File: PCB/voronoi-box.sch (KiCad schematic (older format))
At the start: 31 parts, among them J1 Conn_01x02_Male, J2 Conn_01x02_Male, J3 Conn_01x03_Female, SW1 SW_Push, SW2 SW_Push, SW3 SW_DIP_x01, U1 ATtiny85-20PU

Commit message: remove old stuff from schematic, add battery protection, add a lot of components to Readme
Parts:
- removed C?: 10uF, Capacitor_SMD:C_0603_1608Metric, symbol Device:C
- removed C? (x3): 22uF, Capacitor_SMD:C_0603_1608Metric, symbol Device:C
- removed D?: LED, symbol Device:LED
- removed L?: 1UH, symbol Device:L
- removed R?: 2R, symbol Device:R
- removed R?: 0.5R, symbol Device:R
- removed R?: 10k, symbol Device:R
- removed R?: 1k, symbol Device:R
- removed SW?: SW_Push, Button_Switch_THT:SW_PUSH_6mm_H4.3mm, symbol Switch:SW_Push
- removed U?: IP5306-I2C, lcsc:ESOP-8_L4.9-W3.9-P1.27-LS6.0-BL-EP2.0, symbol LCSC:IP5306-I2C
- added JP?: SolderJumper_2_Open, symbol Jumper:SolderJumper_2_Open
- added R?: 1k, Resistor_SMD:R_0603_1608Metric_Pad1.05x0.95mm_HandSolder, symbol Device:R
- added R?: 2k, Resistor_SMD:R_0603_1608Metric_Pad1.05x0.95mm_HandSolder, symbol Device:R
- added R?: 1M, Resistor_SMD:R_0603_1608Metric_Pad1.05x0.95mm_HandSolder, symbol Device:R
- added R?: 4k, Resistor_SMD:R_0603_1608Metric_Pad1.05x0.95mm_HandSolder, symbol Device:R
- added R?: 8k, Resistor_SMD:R_0603_1608Metric_Pad1.05x0.95mm_HandSolder, symbol Device:R
- added SW? (x3): SW_Push, Button_Switch_THT:SW_PUSH_6mm_H4.3mm, symbol Switch:SW_Push
- added U?: XB8089D0, lcsc:SOIC-8_L4.9-W3.9-P1.27-LS6.0-BL-EP3.3-1, symbol LCSC:XB8089D0
- C?: value 22uF -> 0.1uF
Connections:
- net labels added: BAT+, BAT-, BAT_-, CHRG_+, CHRG_-
- net labels removed: +BATT
- wire segments 43 -> 50
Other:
- note added: "..."
- note added: "// How can it be good to have a resistor in series??"
- note added: "<= 8 MHz with any precision, so it doesn't need external oscillator\n-> set via chip fuses\n\nVBAT can be measured from VCC, keep AREF floating\n\nPB1 can PWM, PB2 has INT0, all have internal pull-up."
- note added: "Battery Protection (Optional)\n4.25 V -> 4.10 V | 2.90 V-> 3.0 V | 10.0 A"
- note added: "TODO:\n- switch via connector?"
- note added: "bridge to bypass BMS"
- note removed: "<= 8 MHz with any precision, so it doesn't need external oscillator\n-> set via chip fuses\n\nVBAT can be measured from VCC, keep AREF floating\n\nPB2 has INT0, PB1 can PWM, all have internal pull-up."
- note removed: "TODO:\n- switch via connector?\n\nIP5306:\n- Optocoupler or direct IO? "Flashlight" mode dangerous. Might work by load alone.\n- LED indicator disable or to IO?\n- No Charge control without I2C -> connect via bus? Would open up AREF"
- moved on the sheet: C?, D1, F1, J1, SW1, SW2, SW3

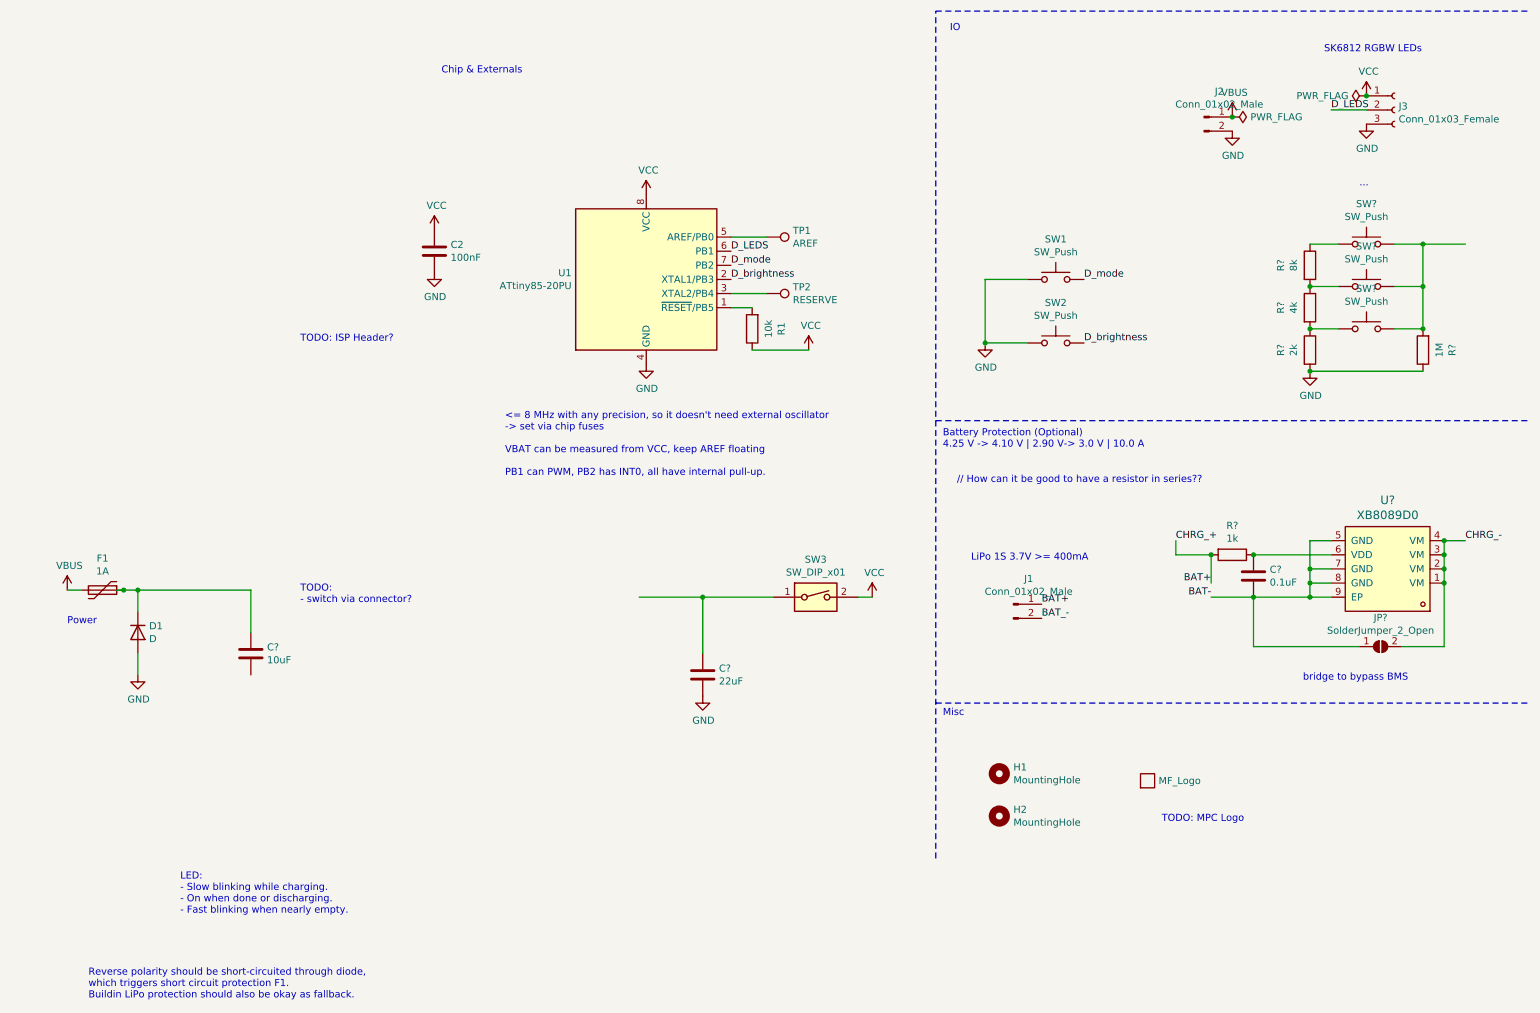
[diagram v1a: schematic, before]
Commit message: extend Readme with a huge knowledge drop, create new power path with dedicated parts, add ISP, use analog mux for buttons, try to fix CI
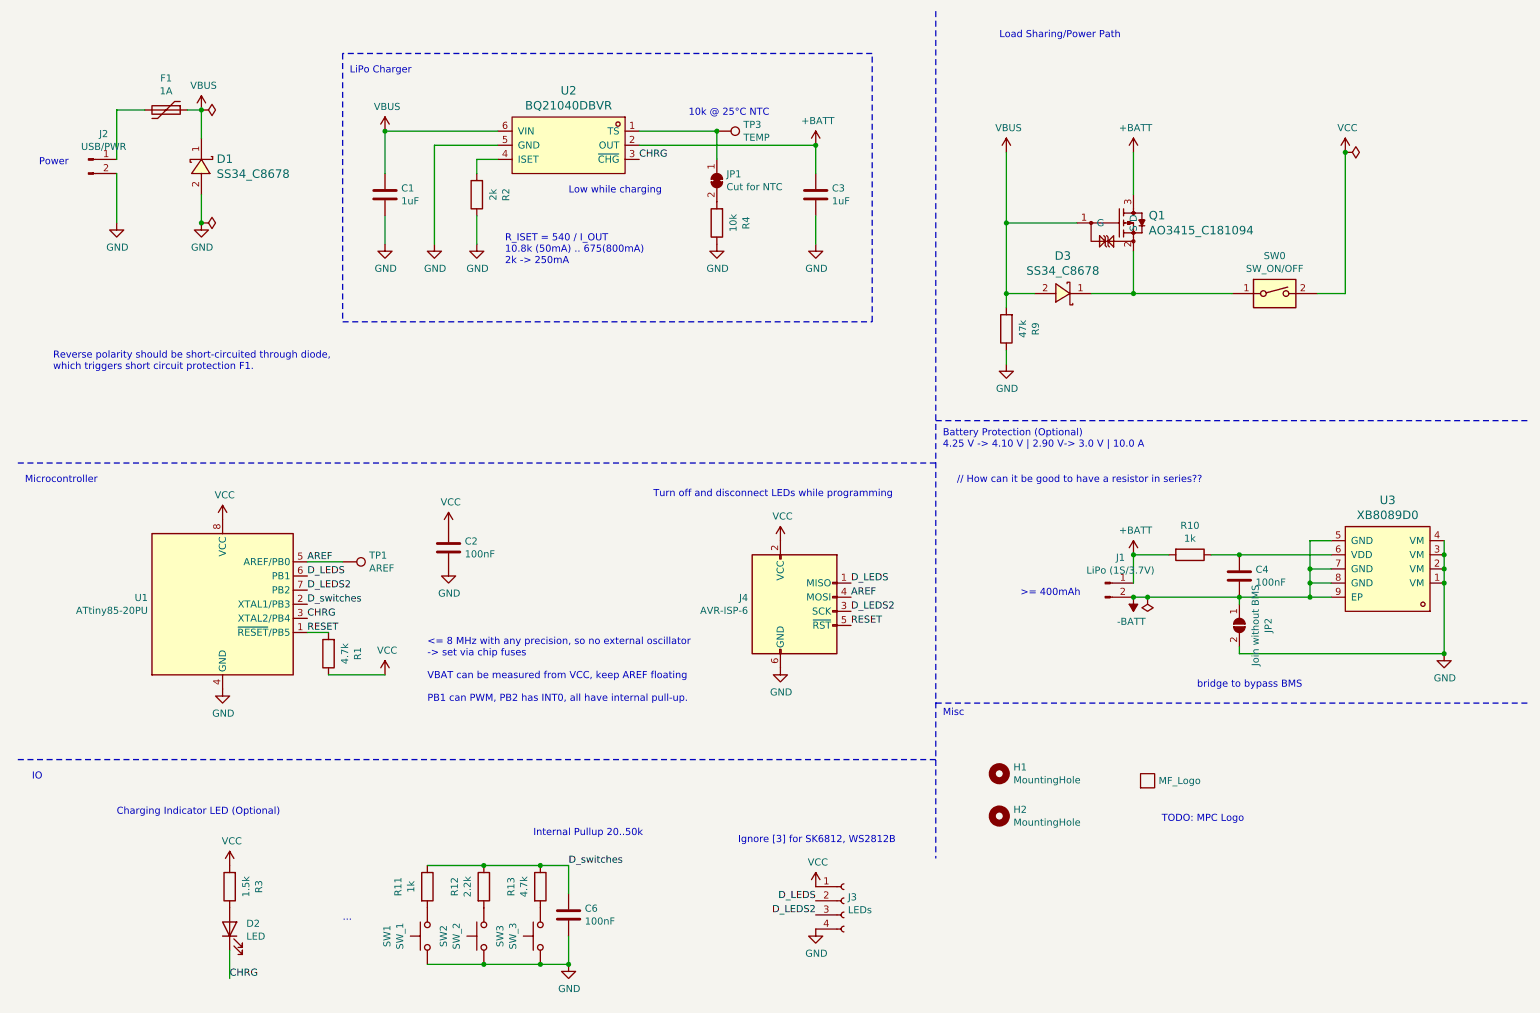
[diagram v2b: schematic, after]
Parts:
- removed C?: 22uF, Capacitor_SMD:C_0603_1608Metric, symbol Device:C
- removed D1: D, Diode_THT:D_DO-35_SOD27_P7.62mm_Horizontal, symbol Device:D
- removed J3: Conn_01x03_Female, Connector_JST:JST_XH_S3B-XH-A_1x03_P2.50mm_Horizontal, symbol Connector:Conn_01x03_Female
- removed R?: 2k, Resistor_SMD:R_0603_1608Metric_Pad1.05x0.95mm_HandSolder, symbol Device:R
- removed R?: 1M, Resistor_SMD:R_0603_1608Metric_Pad1.05x0.95mm_HandSolder, symbol Device:R
- removed R?: 4k, Resistor_SMD:R_0603_1608Metric_Pad1.05x0.95mm_HandSolder, symbol Device:R
- removed R?: 8k, Resistor_SMD:R_0603_1608Metric_Pad1.05x0.95mm_HandSolder, symbol Device:R
- removed SW? (x3): SW_Push, Button_Switch_THT:SW_PUSH_6mm_H4.3mm, symbol Switch:SW_Push
- removed TP2: RESERVE, TestPoint:TestPoint_THTPad_D2.0mm_Drill1.0mm, symbol Connector:TestPoint
- added C3: 1uF, Capacitor_SMD:C_0603_1608Metric, symbol Device:C
- added C6: 100nF, Capacitor_SMD:C_0603_1608Metric, symbol Device:C
- added D1, D3: SS34_C8678, lcsc:SMA_L4.3-W2.6-LS5.2-RD, symbol LCSC:SS34_C8678
- added D2: LED, symbol Device:LED
- added J3: LEDs, Connector_JST:JST_XH_B4B-XH-A_1x04_P2.50mm_Vertical, symbol Connector:Conn_01x04_Female
- added J4: AVR-ISP-6, Connector_PinHeader_2.54mm:PinHeader_2x03_P2.54mm_Vertical, symbol Connector:AVR-ISP-6
- added JP1: Cut for NTC, Jumper:SolderJumper-2_P1.3mm_Bridged_RoundedPad1.0x1.5mm, symbol Jumper:SolderJumper_2_Bridged
- added Q1: AO3415_C181094, lcsc:SOT-23-3_L2.9-W1.3-P1.90-LS2.4-BR, symbol LCSC:AO3415_C181094
- added R11: 1k, Resistor_SMD:R_0603_1608Metric_Pad1.05x0.95mm_HandSolder, symbol Device:R
- added R12: 2.2k, Resistor_SMD:R_0603_1608Metric_Pad1.05x0.95mm_HandSolder, symbol Device:R
- added R13: 4.7k, Resistor_SMD:R_0603_1608Metric_Pad1.05x0.95mm_HandSolder, symbol Device:R
- added R2: 2k, Resistor_SMD:R_0603_1608Metric_Pad1.05x0.95mm_HandSolder, symbol Device:R
- added R3: 1.5k, Resistor_SMD:R_0603_1608Metric_Pad1.05x0.95mm_HandSolder, symbol Device:R
- added R4: 10k, Resistor_SMD:R_0603_1608Metric_Pad1.05x0.95mm_HandSolder, symbol Device:R
- added R9: 47k, Resistor_SMD:R_0603_1608Metric_Pad1.05x0.95mm_HandSolder, symbol Device:R
- added SW3: SW_3, Button_Switch_THT:SW_PUSH_6mm_H4.3mm, symbol Switch:SW_Push
- added TP3: TEMP, TestPoint:TestPoint_THTPad_D2.0mm_Drill1.0mm, symbol Connector:TestPoint
- added U2: BQ21040DBVR, lcsc:SOT-23-6_L2.9-W1.6-P0.95-LS2.8-BR, symbol LCSC:BQ21040DBVR
- C1: renamed from C?; value 10uF -> 1uF
- C4: renamed from C?; value 0.1uF -> 100nF
- J1: value Conn_01x02_Male -> LiPo (1S/3.7V)
- J2: value Conn_01x02_Male -> USB/PWR
- JP2: renamed from JP?; value SolderJumper_2_Open -> Join without BMS; footprint (none) -> Jumper:SolderJumper-2_P1.3mm_Open_RoundedPad1.0x1.5mm
- R1: value 10k -> 4.7k
- SW0: renamed from SW3; value SW_DIP_x01 -> SW_ON/OFF
- SW1: value SW_Push -> SW_1
- SW2: value SW_Push -> SW_2
- gave numbers to parts that had none: 2
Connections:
- net labels added: +BATT, -BATT, AREF, CHRG, D_LEDS2, D_switches, RESET
- net labels removed: BAT+, BAT-, BAT_-, CHRG_+, CHRG_-, D_brightness, D_mode
- wire segments 50 -> 64
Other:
- note added: "10k @ 25°C NTC"
- note added: "<= 8 MHz with any precision, so no external oscillator\n-> set via chip fuses\n\nVBAT can be measured from VCC, keep AREF floating\n\nPB1 can PWM, PB2 has INT0, all have internal pull-up."
- note added: ">= 400mAh"
- note added: "Charging Indicator LED (Optional)"
- note added: "Ignore [3] for SK6812, WS2812B"
- note added: "Internal Pullup 20..50k"
- note added: "LiPo Charger"
- note added: "Load Sharing/Power Path"
- note added: "Low while charging"
- note added: "Microcontroller"
- note added: "R_ISET = 540 / I_OUT\n10.8k (50mA) .. 675(800mA)\n2k -> 250mA"
- note added: "Reverse polarity should be short-circuited through diode, \nwhich triggers short circuit protection F1."
- note added: "Turn off and disconnect LEDs while programming"
- note removed: "<= 8 MHz with any precision, so it doesn't need external oscillator\n-> set via chip fuses\n\nVBAT can be measured from VCC, keep AREF floating\n\nPB1 can PWM, PB2 has INT0, all have internal pull-up."
- note removed: "Chip & Externals"
- note removed: "LED: \n- Slow blinking while charging. \n- On when done or discharging. \n- Fast blinking when nearly empty."
- note removed: "LiPo 1S 3.7V >= 400mA"
- note removed: "Reverse polarity should be short-circuited through diode, \nwhich triggers short circuit protection F1. \nBuildin LiPo protection should also be okay as fallback."
- note removed: "SK6812 RGBW LEDs"
- note removed: "TODO: ISP Header?"
- note removed: "TODO:\n- switch via connector?"
- moved on the sheet: C1, C2, C4, F1, J1, J2, JP2, R1, R10, SW0, TP1, U1

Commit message: add more readme comments and links, add capacitors and more part numbers, fix lib ref
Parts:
- added C5, C7: 22uF, Capacitor_SMD:C_0603_1608Metric, symbol Device:C
- added JP3: Cut for LED, Jumper:SolderJumper-2_P1.3mm_Bridged_RoundedPad1.0x1.5mm, symbol Jumper:SolderJumper_2_Bridged
- added TP2: PB4, TestPoint:TestPoint_THTPad_D2.0mm_Drill1.0mm, symbol Connector:TestPoint
- C1, C3: JLC Part (none) -> Basic Part; LCSC Part (none) -> C15849
- C2, C4, C6: JLC Part (none) -> Basic Part; LCSC Part (none) -> C14663
- D2: footprint (none) -> LED_SMD:LED_1206_3216Metric_Pad1.42x1.75mm_HandSolder
- F1: value 1A -> 1.5A; LCSC Part (none) -> C883133
- H1, H2: footprint MountingHole:MountingHole_3.2mm_M3_DIN965 -> MountingHole:MountingHole_3.2mm_M3_Pad
- J1, J2: symbol Connector:Conn_01x02_Male -> Connector_Generic:Conn_01x02
- J3: symbol Connector:Conn_01x04_Female -> Connector_Generic:Conn_01x04
- J4: value AVR-ISP-6 -> AVR-ISP
- R1, R13: JLC Part (none) -> Basic Part; LCSC Part (none) -> C23162
- R10, R11: JLC Part (none) -> Basic Part; LCSC Part (none) -> C21190
- R12: JLC Part (none) -> Basic Part; LCSC Part (none) -> C4190
- R2: value 2k -> 2.2k; JLC Part (none) -> Basic Part; LCSC Part (none) -> C4190
- R3: JLC Part (none) -> Basic Part; LCSC Part (none) -> C22843
- R4: JLC Part (none) -> Basic Part; LCSC Part (none) -> C25804
- R9: JLC Part (none) -> Basic Part; LCSC Part (none) -> C25819
- U1: LCSC Part (none) -> *
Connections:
- net CHRG: now also JP3.2 (B); no longer U1.3 (XTAL2/PB4)
- net GND: now also C5.2, C7.2
- net VBUS: now also C7.1
- net VCC: now also C5.1
- new net: JP3.1 (A), TP2.1, U1.3 (XTAL2/PB4)
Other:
- note added: "Low while charging\nUse LED or PB4"
- note added: "R_ISET = 540 / I_OUT\n10.8k (50mA) .. 675(800mA)\n2.2k -> 250mA"
- note added: "TODO: Check pins"
- note added: "TODO: Check polarity"
- note added: "TODO: TVS?"
- note added: "TODO: rename"
- note removed: "Low while charging"
- note removed: "R_ISET = 540 / I_OUT\n10.8k (50mA) .. 675(800mA)\n2k -> 250mA"
- moved on the sheet: C1, C2, C3, C6, D1, D2, D3, F1, JP1, Q1, R1, R11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
